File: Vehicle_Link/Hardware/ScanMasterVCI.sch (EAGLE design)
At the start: 88 parts, among them IC1 XMEGA32A4U, Q1 MMBT4403, Q10 ZXMP6A17G, Q2 MMBT3904, Q3 MMBT3904, Q4 MMBT3904, Q5 MMBT3904, Q6 MMBT3904, Q7 NTZD5110N, Q8 NTZD5110N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

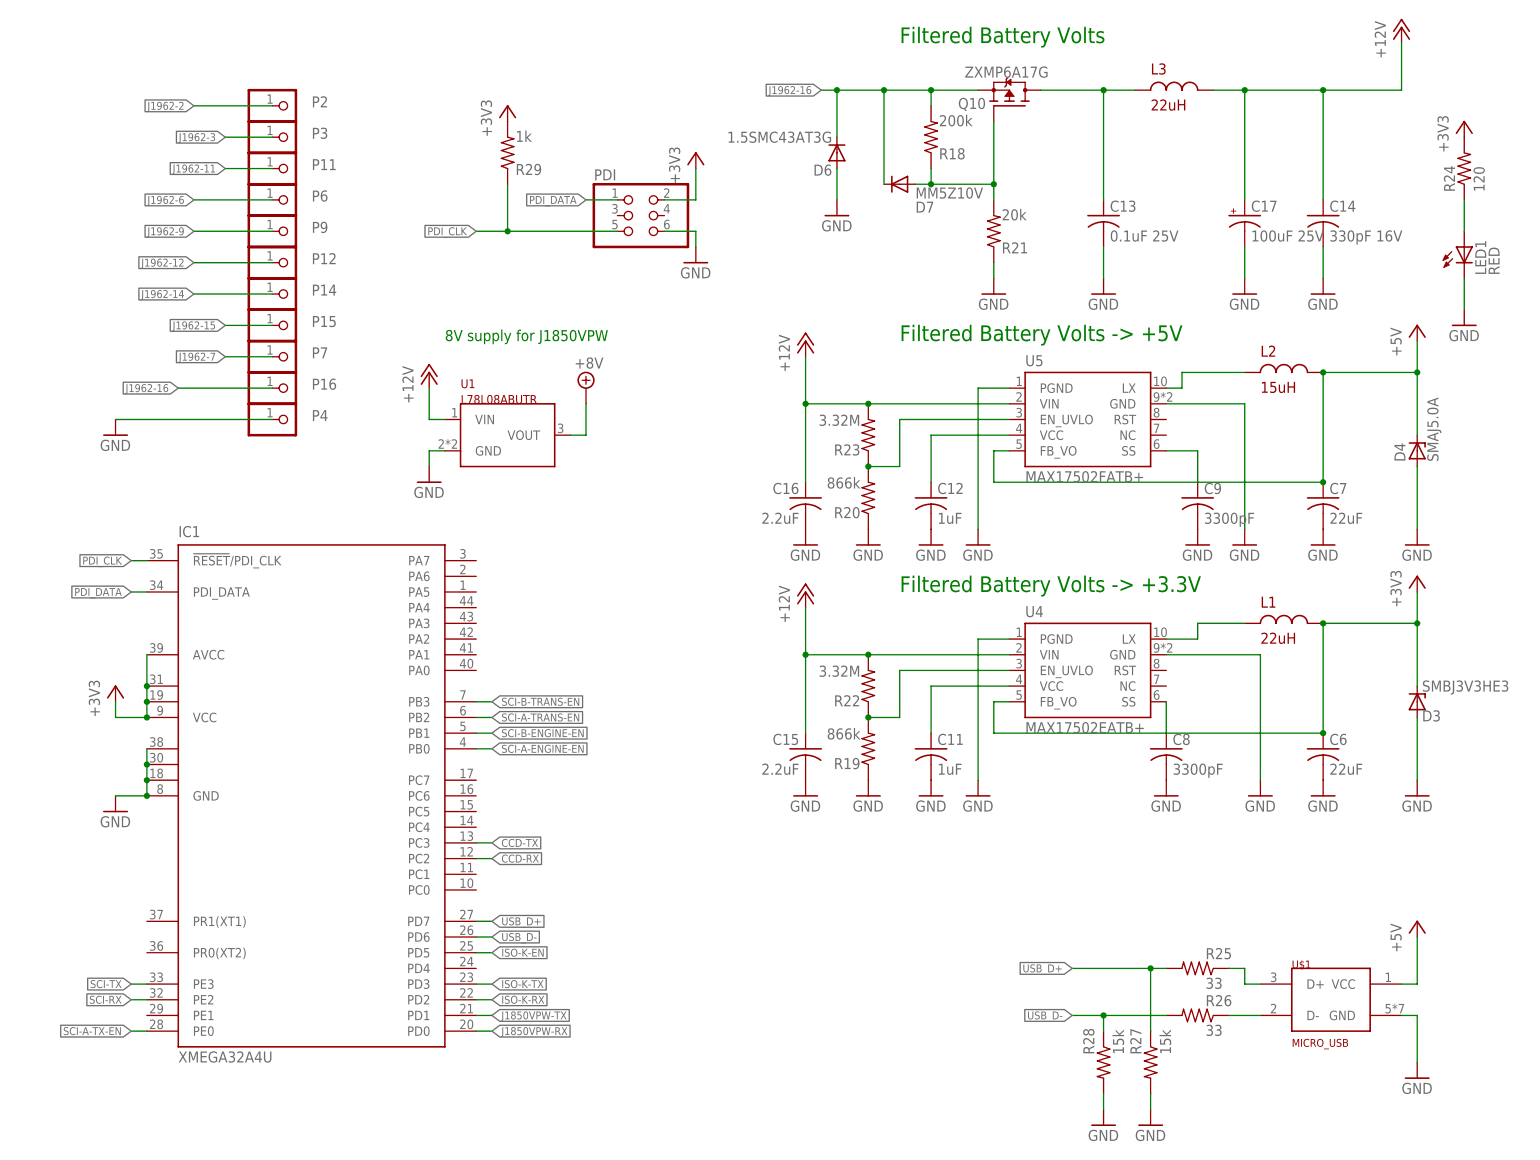
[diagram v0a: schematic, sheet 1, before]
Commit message: Added LED. Fixed soldering issues. 8V IC pins were wrong.
Added an LED for comm indication. Added resistor for this LED. The L78L pinout had VIN and VOUT swapped somehow, fixed this. The MAX17502 has proven very difficult to solder, even with paste. The pad below the chip causes bridging in extreme cases so I fixed that as well.
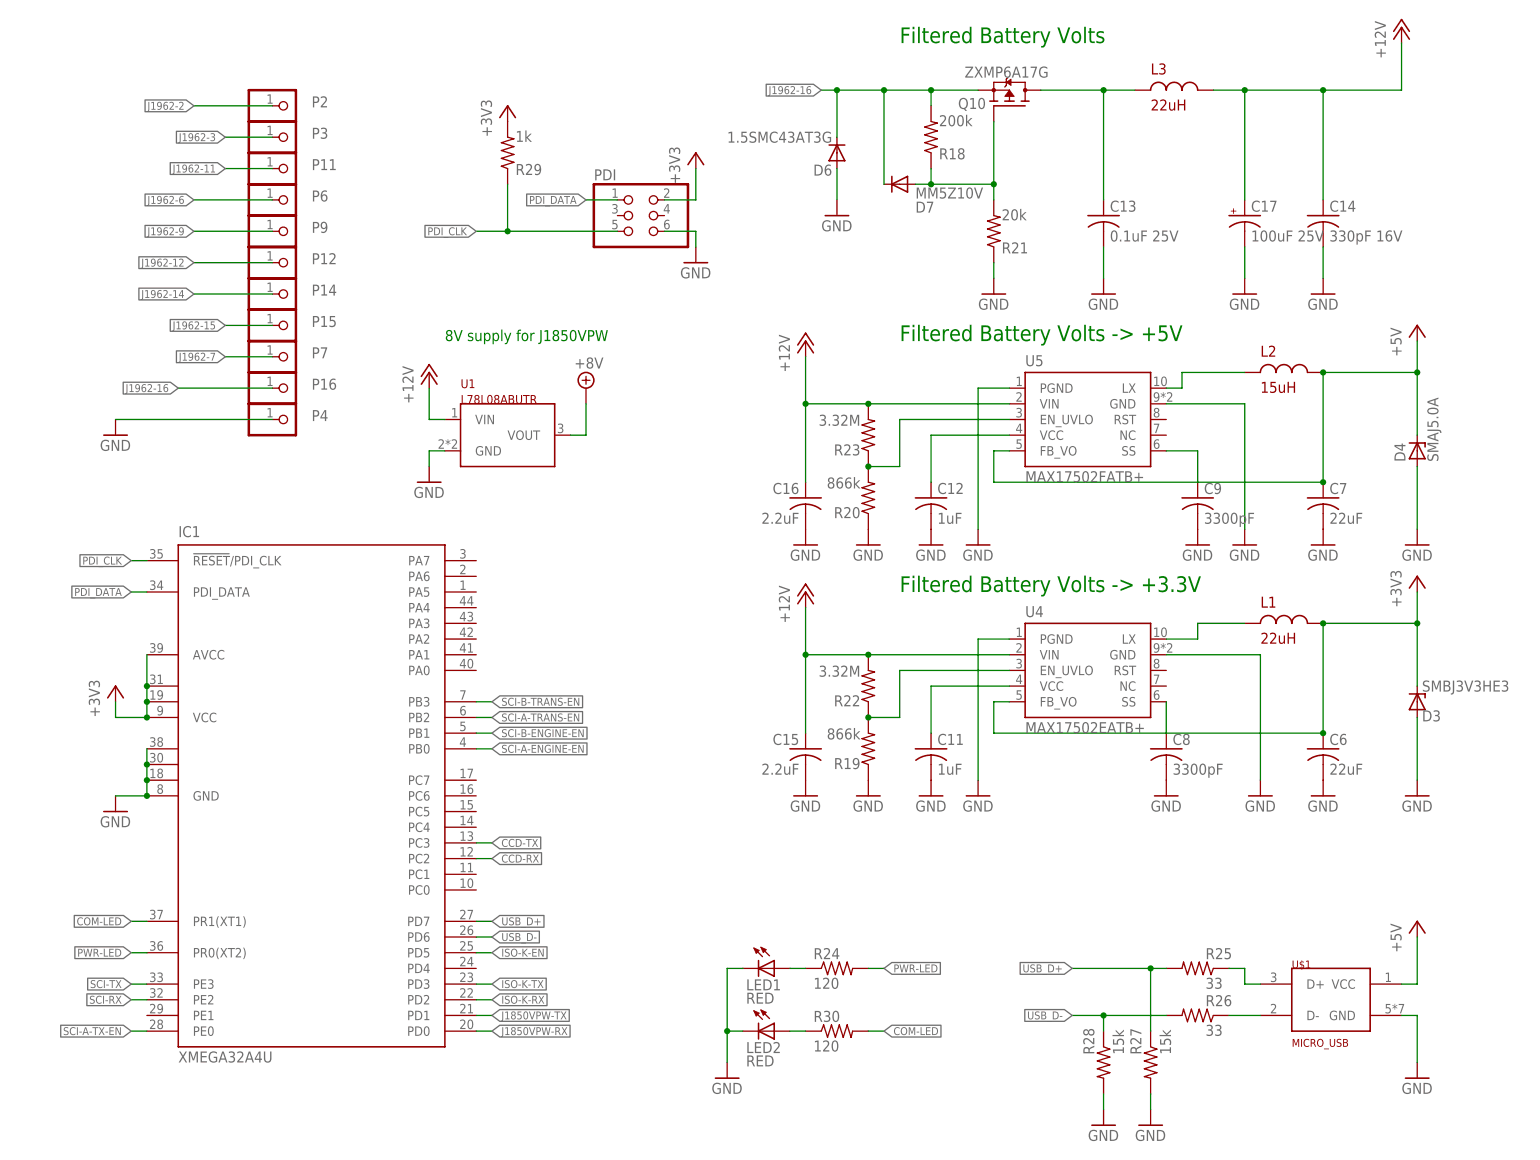
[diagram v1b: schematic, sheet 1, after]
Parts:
- added LED2: RED, led:LEDCHIP-LED0603
- added R30: 120, resistor:R-US_R0603
- Q7, Q8: value NTZD5110N -> NDC7002N; device customics:NTZD5110N -> customics:NDC7002N
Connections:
- new net COM-LED: IC1.PR1(XT1), R30.2
- new net N$27: LED2.A, R30.1
- new net PWR-LED: IC1.PR0(XT2), R24.2
- net +3V3: no longer R24.2
- net GND: now also LED2.C
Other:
- moved on the sheet: LED1, R24

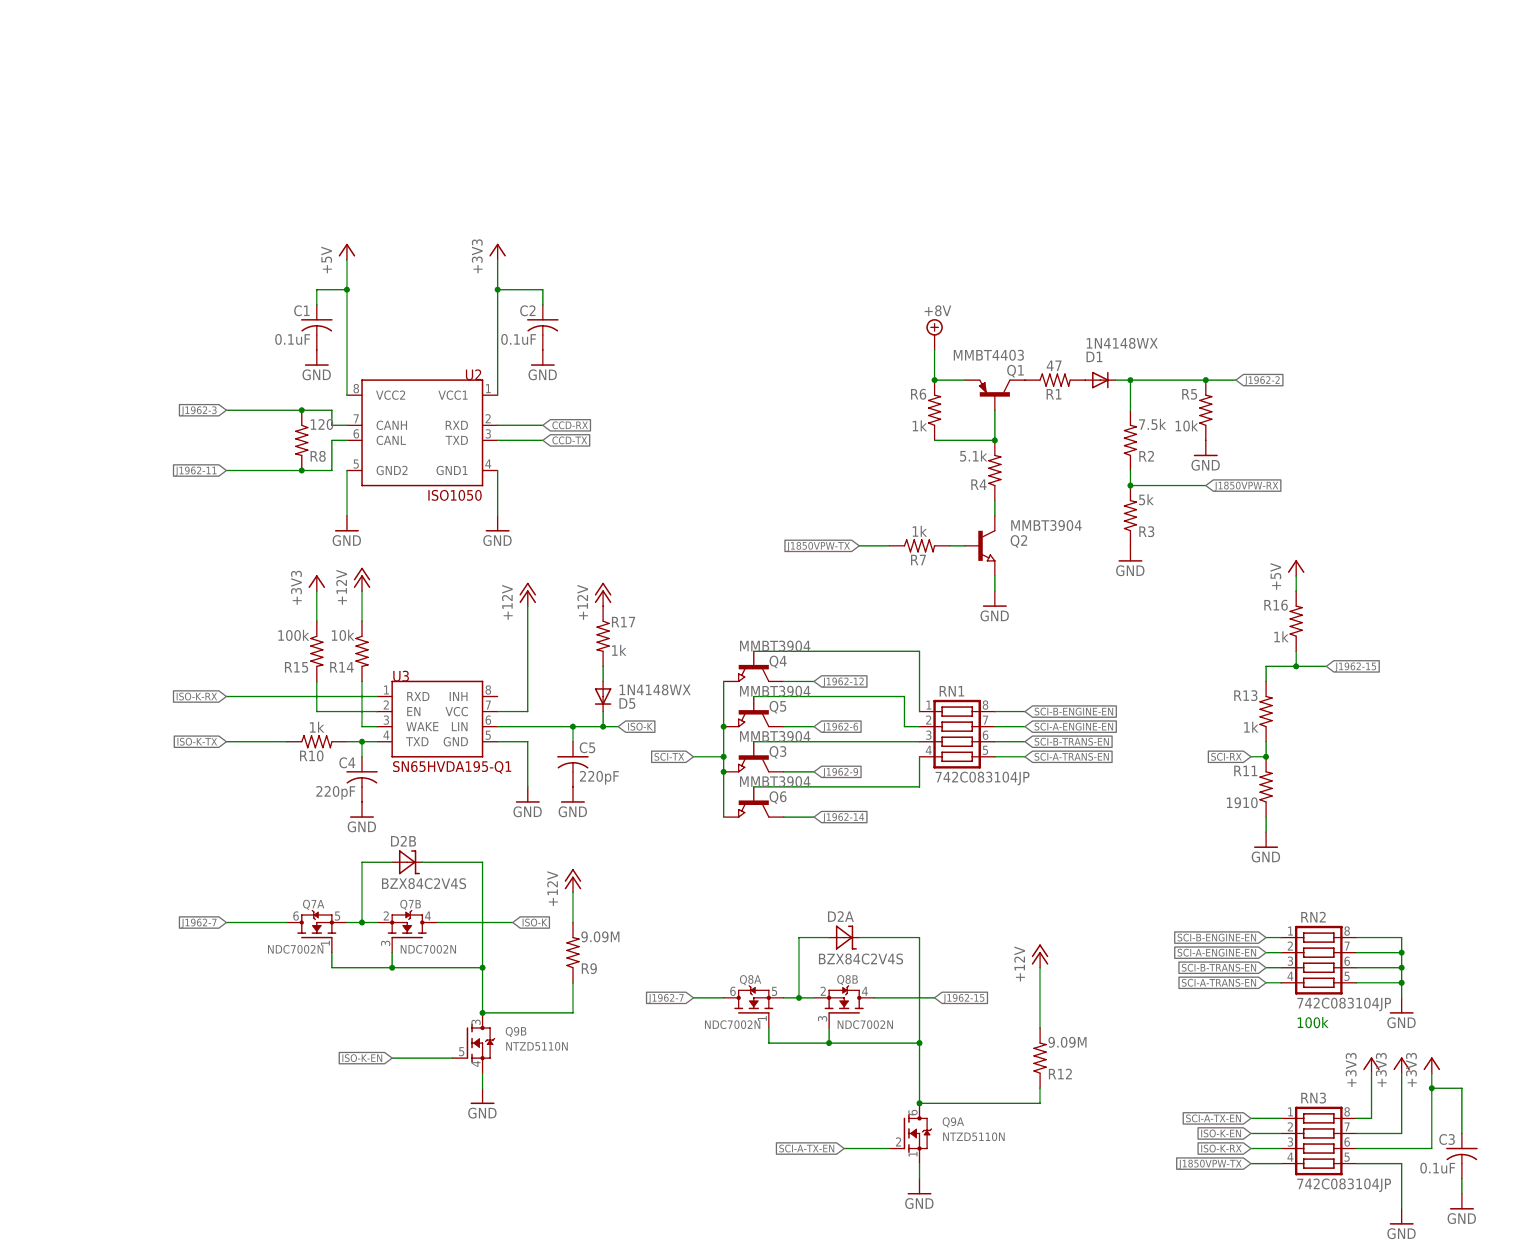
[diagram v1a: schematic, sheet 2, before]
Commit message: Scrubbed ISO1050 from board, replaced with MAX13444EASA+
Using the CAN tranceiver was not working with CCD, so I've gone with an RS-485 IC instead. I've tested this IC with CCD and can confirm it works for reading.
Started the process of removing the device names from the board view, instead I will be showing the values for resistors, capacitors, and inductors, for ease of assembly.
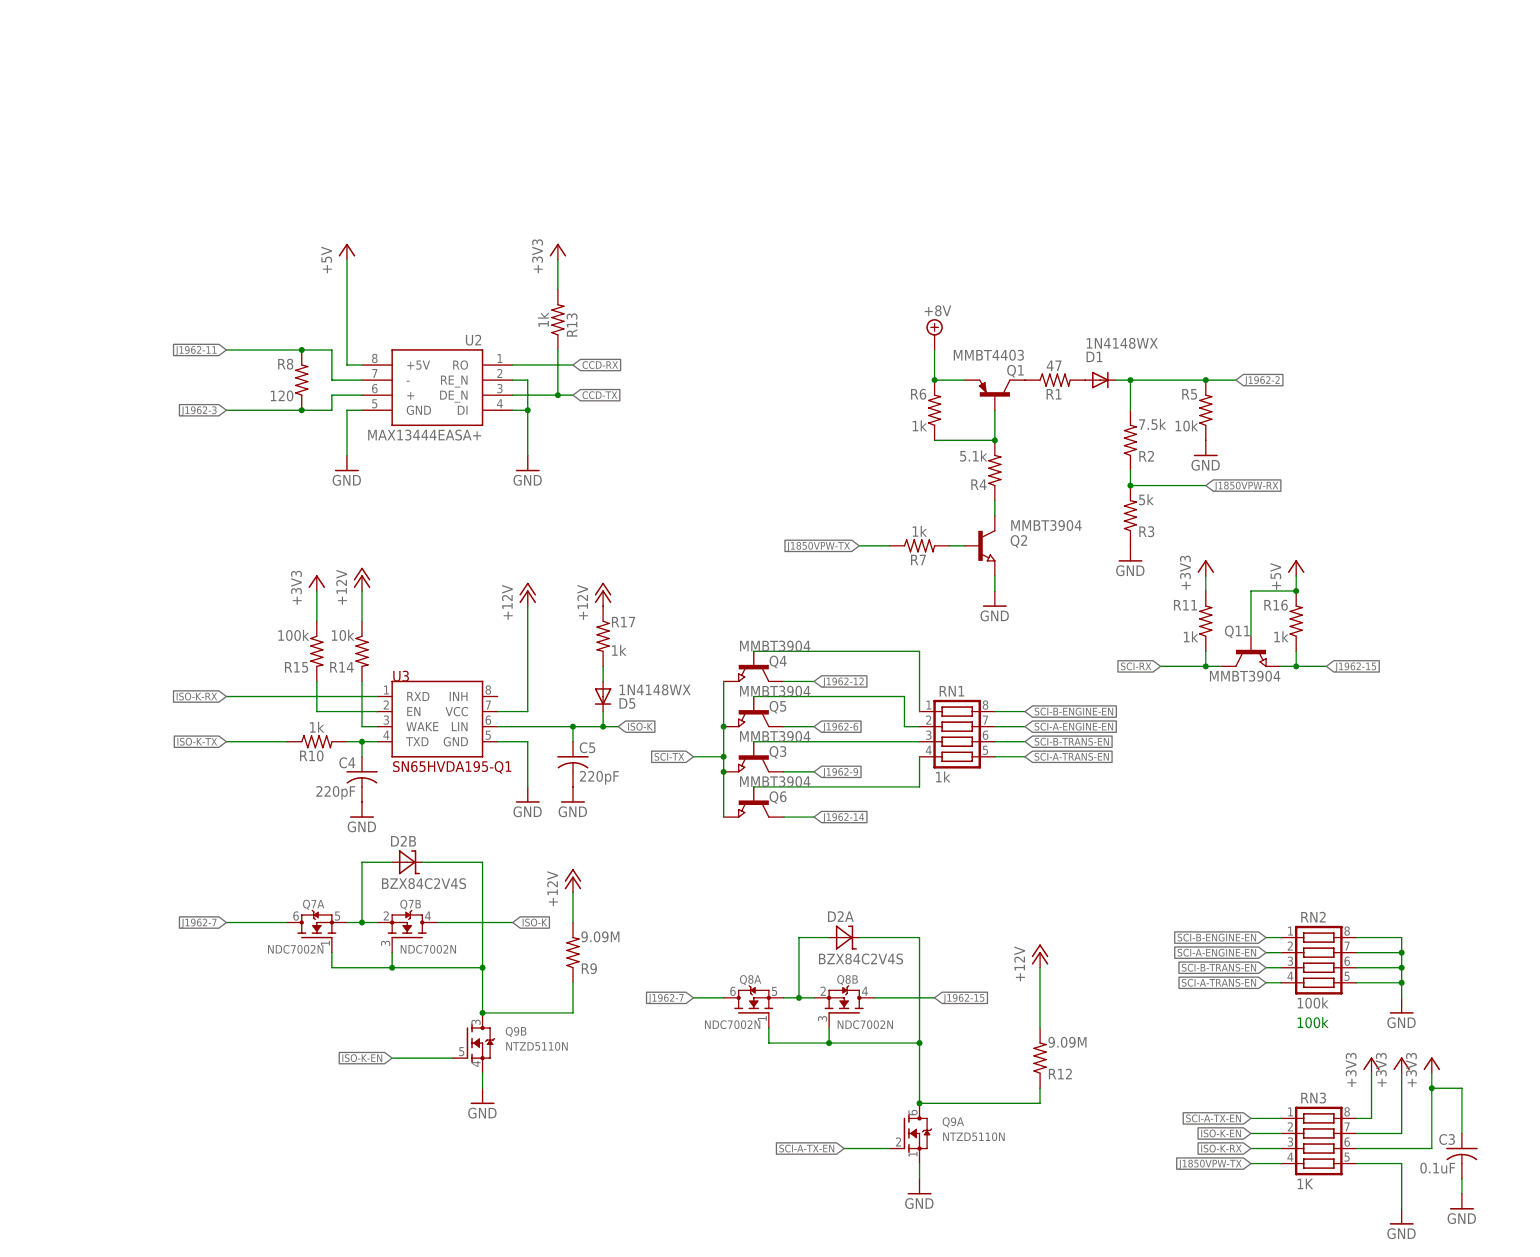
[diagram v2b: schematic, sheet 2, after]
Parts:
- removed C1, C2: 0.1uF, adafruit:C-USC0603
- added Q11: MMBT3904, semicon-smd-ipc:NPN-TRANSISTOR_SOT23
- C8, C9: value 3300pF -> 3.3nF
- R11: value 1910 -> 1k
- RN1: value 742C083104JP -> 1k
- RN2: value 742C083104JP -> 100k
- RN3: value 742C083104JP -> 1K
- U2: value ISO1050 -> MAX13444EASA+; device customics:ISO1050 -> customics:MAX13444EASA+SMD
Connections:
- net +3V3: now also R11.2, R13.2; no longer C2.1, U2.VCC1
- net +5V: now also Q11.B, U2.+5V; no longer C1.1, U2.VCC2
- net CCD-RX: now also U2.RO; no longer U2.RXD
- net CCD-TX: now also R13.1, U2.DE_N; no longer U2.TXD
- net GND: now also U2.DI, U2.GND, U2.RE_N; no longer C1.2, C2.2, R11.1, U2.GND1, U2.GND2
- net J1962-11: now also U2.-; no longer U2.CANL
- net J1962-15: now also Q11.E; no longer R13.2
- net J1962-3: now also U2.+; no longer U2.CANH
- net SCI-RX: now also Q11.C, R11.1; no longer R11.2, R13.1
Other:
- moved on the sheet: R11, R13, R8, U2

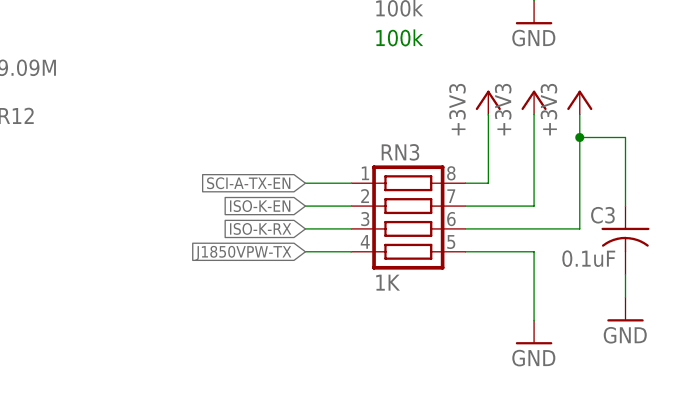
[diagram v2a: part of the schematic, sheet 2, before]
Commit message: Finished replacing names with values on the board view. Resistors, capacitors and inductors all should be showing the values instead of the names on the board view. This makes organizing parts for assembly much easier.
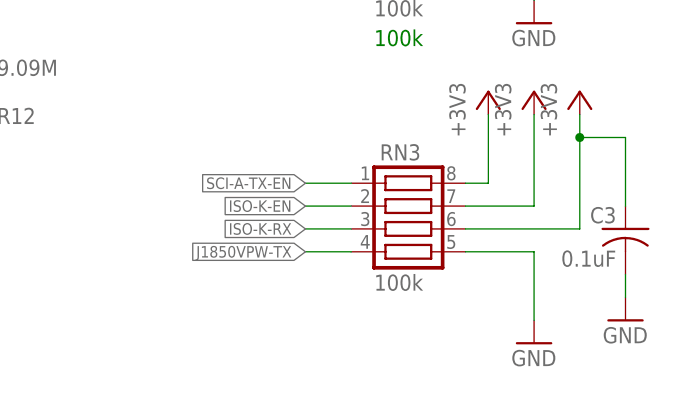
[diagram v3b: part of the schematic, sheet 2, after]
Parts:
- RN3: value 1K -> 100k
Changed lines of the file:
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@@
 <?xml version="1.0" encoding="utf-8"?>
 <!DOCTYPE eagle SYSTEM "eagle.dtd">
-<eagle version="8.4.3">
+<eagle version="8.7.0">
 <drawing>
 <settings>
@@
 <part name="Q7" library="customics" deviceset="NDC7002N" device=""/>
 <part name="Q8" library="customics" deviceset="NDC7002N" device=""/>
-<part name="RN3" library="resistor-net" library_urn="urn:adsk.eagle:library:343" deviceset="CTS742C083" device="" package3d_urn="urn:adsk.eagle:package:24985/1" value="1K"/>
+<part name="RN3" library="resistor-net" library_urn="urn:adsk.eagle:library:343" deviceset="CTS742C083" device="" package3d_urn="urn:adsk.eagle:package:24985/1" value="100k"/>
 <part name="GND37" library="supply1" library_urn="urn:adsk.eagle:library:371" deviceset="GND" device=""/>
 <part name="+3V9" library="supply1" library_urn="urn:adsk.eagle:library:371" deviceset="+3V3" device=""/>
